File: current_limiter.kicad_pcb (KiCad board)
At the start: 4 copper layers, 83.9 x 37.5 mm, 49 parts, among them J1 73096-2, J2 73096-2, J3 CS-, J4 CS+, J5 73096-2, J6 73096-2, Q1 BSC040N10NS5, Q2 BC849, Q3 BC858, U1 TLV1805QDBVRQ1, U2 INA181A2IDBVR, U3 OPA991IDCKR, U4 BAT54CLT3G, U5 LM4040DIM3-2.5/NOPB

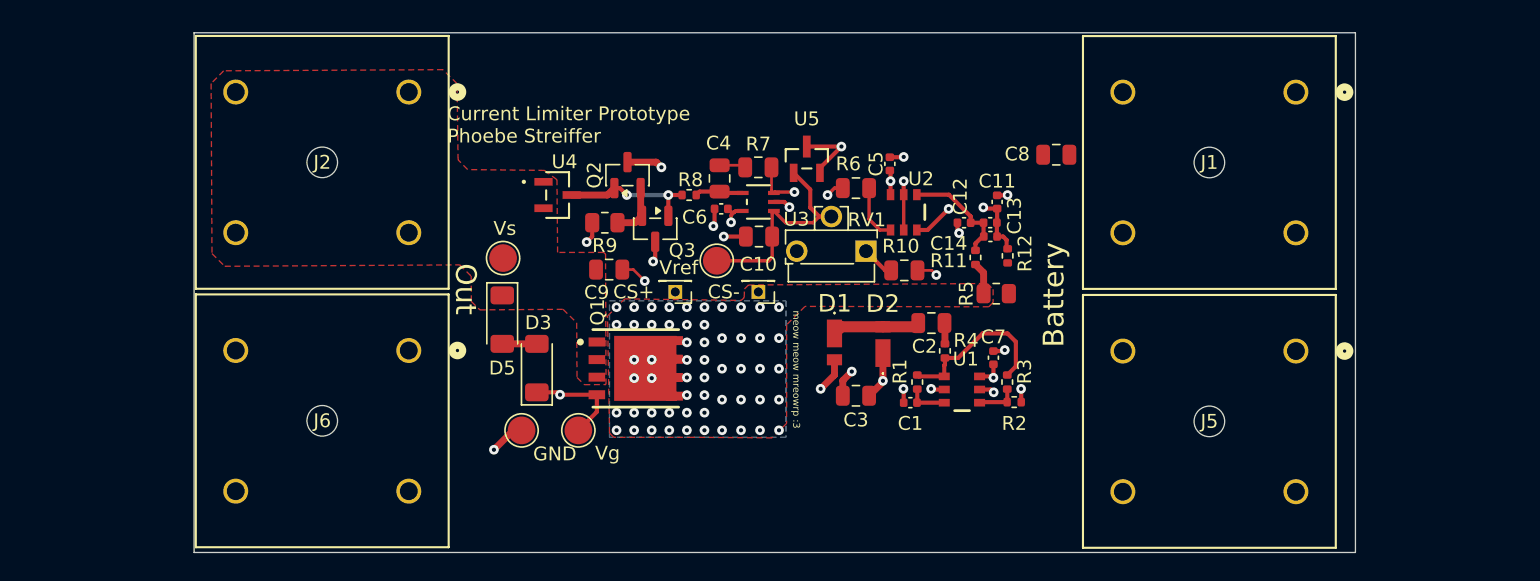
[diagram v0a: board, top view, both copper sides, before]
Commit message: minor revisions: added mounting holes, changed one track to back signal layer
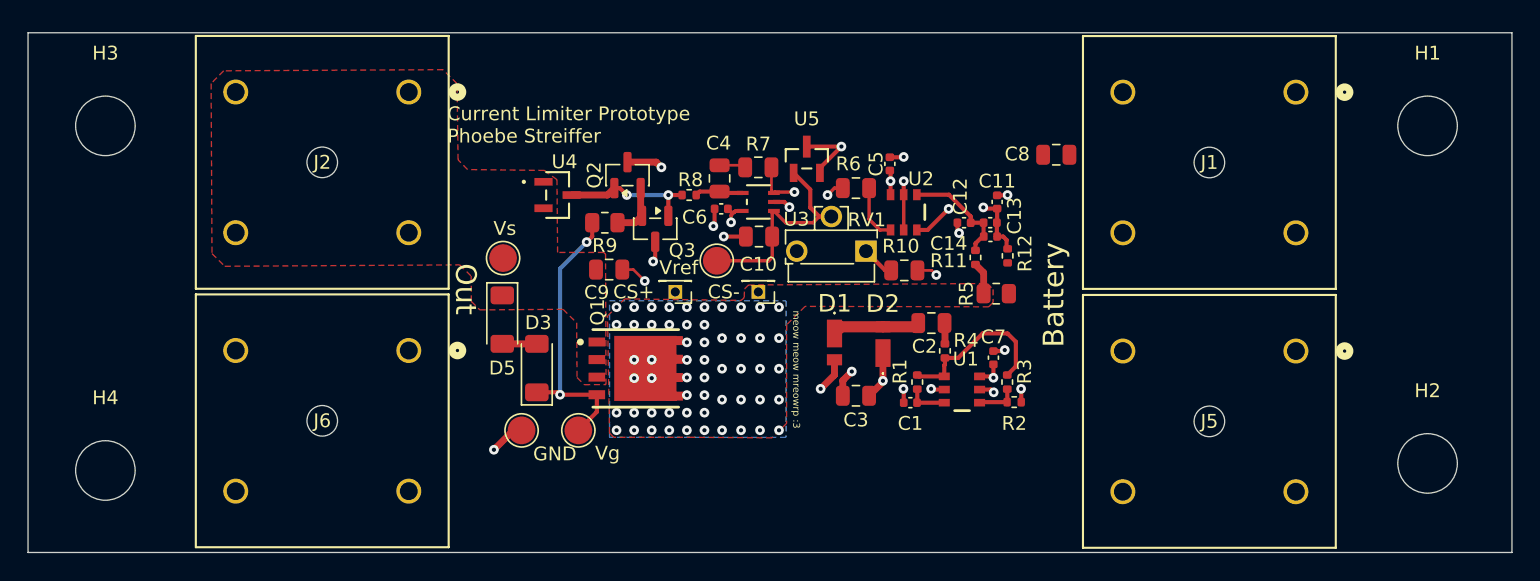
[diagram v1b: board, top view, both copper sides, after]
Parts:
- added H1: MountingHole, MountingHole:MountingHole_4.3mm_M4, F.Cu at (180.3, 32.0)
- added H2: MountingHole, MountingHole:MountingHole_4.3mm_M4, F.Cu at (180.3, 56.4)
- added H3: MountingHole, MountingHole:MountingHole_4.3mm_M4, F.Cu at (84.8, 32.0)
- added H4: MountingHole, MountingHole:MountingHole_4.3mm_M4, F.Cu at (84.8, 56.9)
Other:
- board size 83.9 x 37.5 mm -> 107.2 x 37.5 mm

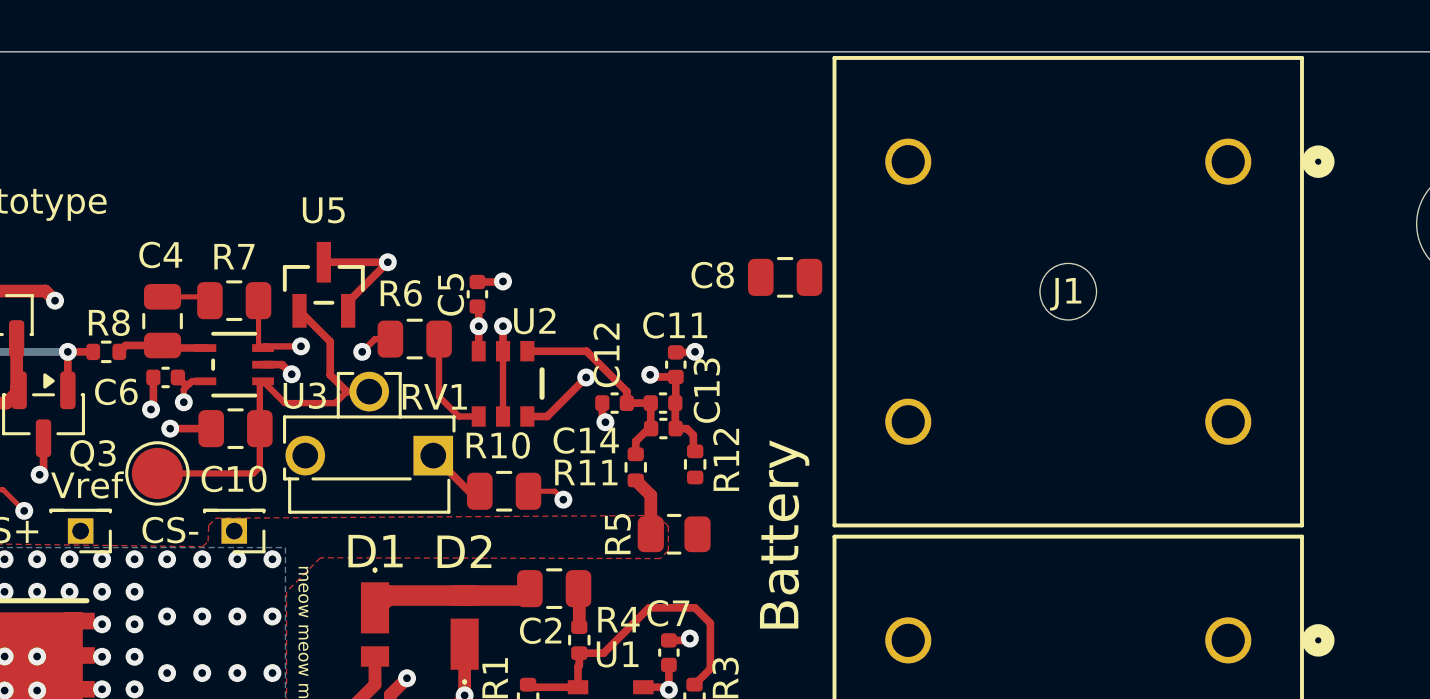
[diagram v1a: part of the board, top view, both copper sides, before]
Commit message: proper shunt setup, properly calculated resistance values necessary for shunt diode to operate safely
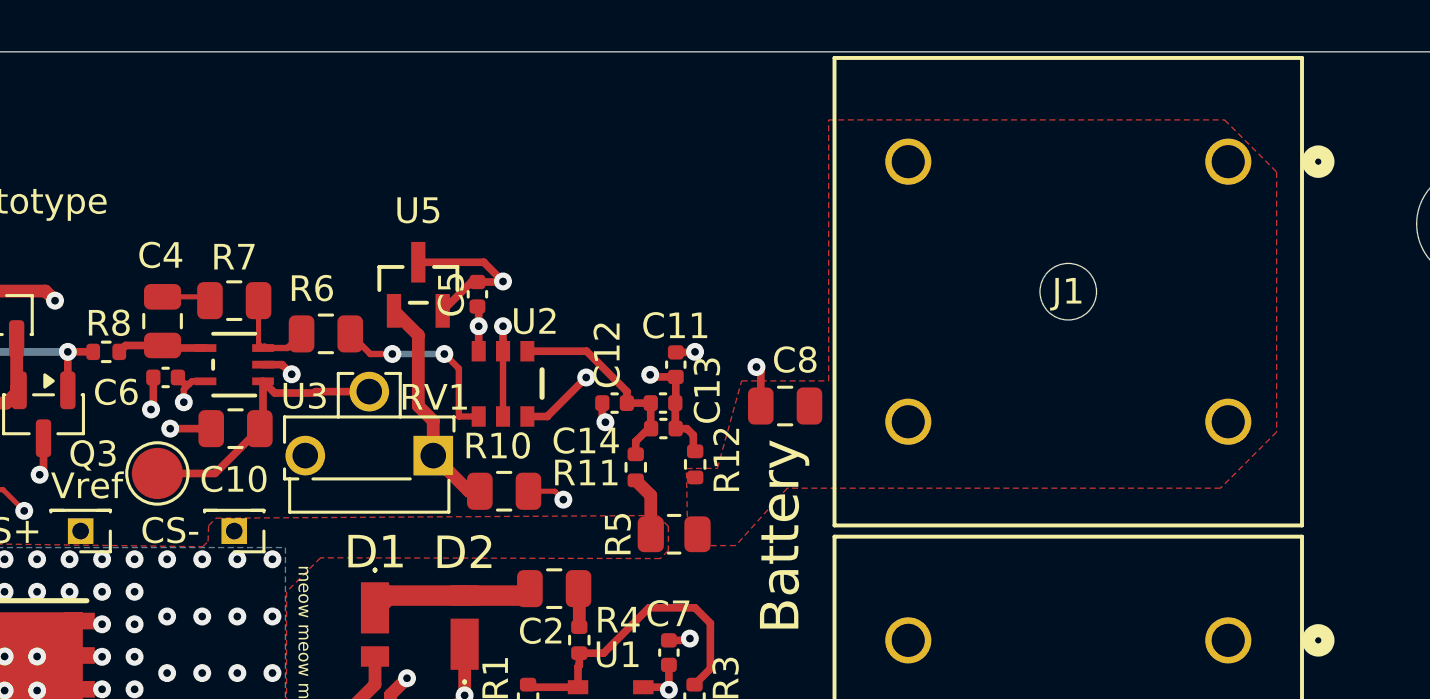
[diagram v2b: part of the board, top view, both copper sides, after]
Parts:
- R10: value 50k -> 20k
- moved C8 5.03 mm to (153.5, 39.1)
- moved U5 3.69 mm to (139.2, 34.4)
- moved R6 3.48 mm to (135.6, 36.3)
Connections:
- C10 pad 2: /REF_SET -> Net-(U3-IN+)
- RV1 pad 2: /REF_SET -> Net-(U3-IN+)
- TP3 pad 1: /REF_SET -> Net-(U3-IN+)
- U3 pad 1: /REF_SET -> Net-(U3-IN+)
- U5 pad 1: /REF_SET -> Net-(R10-Pad1)
- U5 pad 3: unconnected-(U5-Pad3) -> GND
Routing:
- net /REF_SET: track 16.1 -> 0.00 mm
- net Net-(U3-IN+): track 0.00 -> 11.0 mm
- net Net-(R10-Pad1): track 2.71 -> 10.3 mm
- net /PI_IN-: track 7.72 -> 3.75 mm, vias 2 -> 0
- net /CS_OUT: track 4.12 -> 7.45 mm, vias 0 -> 2
- net GND: track 27.7 -> 29.7 mm
- added copper zone on F.Cu, net +15V

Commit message: minor update: changed resistor value from 20k to 22k for E12 value
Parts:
- R10: value 20k -> 22k
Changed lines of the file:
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@@
 			)
 		)
-		(property "Value" "20k"
+		(property "Value" "22k"
 			(at 0 1.68 0)
 			(layer "F.Fab")

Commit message: minor updates: swapped out currentsense for in stock version, made sure all parts in stock, corrected Vs for currentsense
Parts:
- added R13: 22k, Capacitor_SMD:C_0805_2012Metric, F.Cu at (147.4, 34.0)
- added U6: LM4040DIM3-5.0/NOPB, Current_Limiter_Stuff:DBZ3, F.Cu at (143.9, 30.7)
- Q1: value BSC040N10NS5 -> ISC025N08NM5LF2
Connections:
- C5 pad 1: +15V -> Net-(U2-V+)
- U2 pad 6: +15V -> Net-(U2-V+)
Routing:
- net Net-(U2-V+): track 0.00 -> 10.2 mm
- net GND: track 29.7 -> 35.6 mm, vias 17 -> 18

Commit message: updated zeners to model thats actually in stock
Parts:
- removed D3, D5: BZV55B20, Diode_SMD:D_MiniMELF
- added CR1: BZT52C20-7-F, Current_Limiter_Stuff:SOD123_DIO, F.Cu at (113.5, 46.0)
- added CR2: BZT52C20-7-F, Current_Limiter_Stuff:SOD123_DIO, F.Cu at (115.8, 49.6)
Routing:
- net Net-(D3-A): track 2.50 -> 0.00 mm
- net Net-(CR1-Pad2): track 0.00 -> 2.50 mm

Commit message: updated all passive components to 805 footprint, added 3V3 regulator for currentsense
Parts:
- removed C5: 10n, Capacitor_SMD:C_0402_1005Metric
- added C16: 100n, Capacitor_SMD:C_0805_2012Metric, F.Cu at (149.9, 30.0)
- added C17: 100p, Capacitor_SMD:C_0805_2012Metric, F.Cu at (153.9, 34.0)
- added C18: 22u, Capacitor_SMD:C_0805_2012Metric, F.Cu at (143.8, 30.0)
- added C19: 22u, Capacitor_SMD:C_0805_2012Metric, F.Cu at (145.8, 30.0)
- added C20: 100n, Capacitor_SMD:C_0805_2012Metric, F.Cu at (140.2, 35.1)
- added L1: 10u, Inductor_SMD:L_0805_2012Metric, F.Cu at (147.8, 30.0)
- added R14: 22k, Resistor_SMD:R_0805_2012Metric, F.Cu at (139.7, 32.0)
- added R15: 10k, Resistor_SMD:R_0805_2012Metric, F.Cu at (142.5, 41.8)
- C1, C11, C12, C13, C14, C6, C7: footprint Capacitor_SMD:C_0402_1005Metric -> Capacitor_SMD:C_0805_2012Metric
- R1, R11, R12, R2, R3, R4, R8: footprint Resistor_SMD:R_0402_1005Metric -> Resistor_SMD:R_0805_2012Metric
- R10: value 22k -> 30.1k; footprint Capacitor_SMD:C_0805_2012Metric -> Resistor_SMD:R_0805_2012Metric
- R13: value 22k -> 158k; footprint Capacitor_SMD:C_0805_2012Metric -> Resistor_SMD:R_0805_2012Metric
- R6, R7: footprint Capacitor_SMD:C_0805_2012Metric -> Resistor_SMD:R_0805_2012Metric
- U2: value INA181A2IDBVR -> ZXCT181A2W6-7
- U6: value LM4040DIM3-5.0/NOPB -> AP63203QWU-7; footprint Current_Limiter_Stuff:DBZ3 -> Current_Limiter_Stuff:TSOT26_DIO
- moved R10 12.1 mm to (153.4, 37.1), turned to 180 degrees
- moved U6 9.07 mm to (152.9, 30.3), turned to 180 degrees
- moved U5 5.64 mm to (137.7, 29.0), turned to 90 degrees
- moved C12 5.29 mm to (146.8, 33.7), turned to -90 degrees
- moved R13 4.51 mm to (151.9, 34.0), turned to 90 degrees
- moved C11 3.81 mm to (148.8, 33.7)
- moved C14 3.42 mm to (148.8, 36.6)
- moved C1 3.40 mm to (144.2, 55.2), turned to 180 degrees
- moved C7 3.30 mm to (151.9, 50.3), turned to -90 degrees
- moved R3 3.17 mm to (149.5, 53.6), turned to -90 degrees
- moved R4 2.43 mm to (147.8, 47.6)
- moved R2 2.37 mm to (152.4, 53.3)
- moved C4 2.22 mm to (130.6, 34.0)
- moved R1 1.91 mm to (142.9, 52.3)
- moved R8 1.53 mm to (127.5, 35.6)
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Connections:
- R10 pad 1: Net-(R10-Pad1) -> Net-(U6-FB)
- R10 pad 2: +15V -> GND
- R13 pad 1: Net-(U2-V+) -> +3V3
- R13 pad 2: +15V -> Net-(U6-FB)
- RV1 pad 1: Net-(R10-Pad1) -> Net-(R15-Pad1)
- U2 pad 6: Net-(U2-V+) -> +3V3
- U5 pad 1: Net-(R10-Pad1) -> Net-(R14-Pad2)
- U6 pad 1: Net-(U2-V+) -> Net-(U6-FB)
- U6 pad 2: GND -> +15V
- U6 pad 3: GND -> +15V
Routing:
- net +3V3: track 0.00 -> 22.2 mm
- net Net-(R14-Pad2): track 0.00 -> 15.2 mm, vias 0 -> 2
- net Net-(R10-Pad1): track 10.3 -> 0.00 mm
- net Net-(U2-V+): track 10.2 -> 0.00 mm
- net Net-(U6-FB): track 0.00 -> 8.74 mm
- net /CS_FILTERED+: track 10.4 -> 17.5 mm
- net /OSC_OUT: track 12.1 -> 18.2 mm, vias 0 -> 2
- net GND: track 35.6 -> 41.6 mm, vias 18 -> 19
- net Net-(U6-SW): track 0.00 -> 4.38 mm
- net Net-(R15-Pad1): track 0.00 -> 4.22 mm
- net /CS_FILTERED-: track 8.03 -> 10.6 mm
- net Net-(U6-BST): track 0.00 -> 1.88 mm
- net +15V: track 7.29 -> 9.17 mm, vias 4 -> 3
- net /BASE: track 9.89 -> 11.4 mm
- net /OSC_IN+: track 2.96 -> 4.38 mm
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
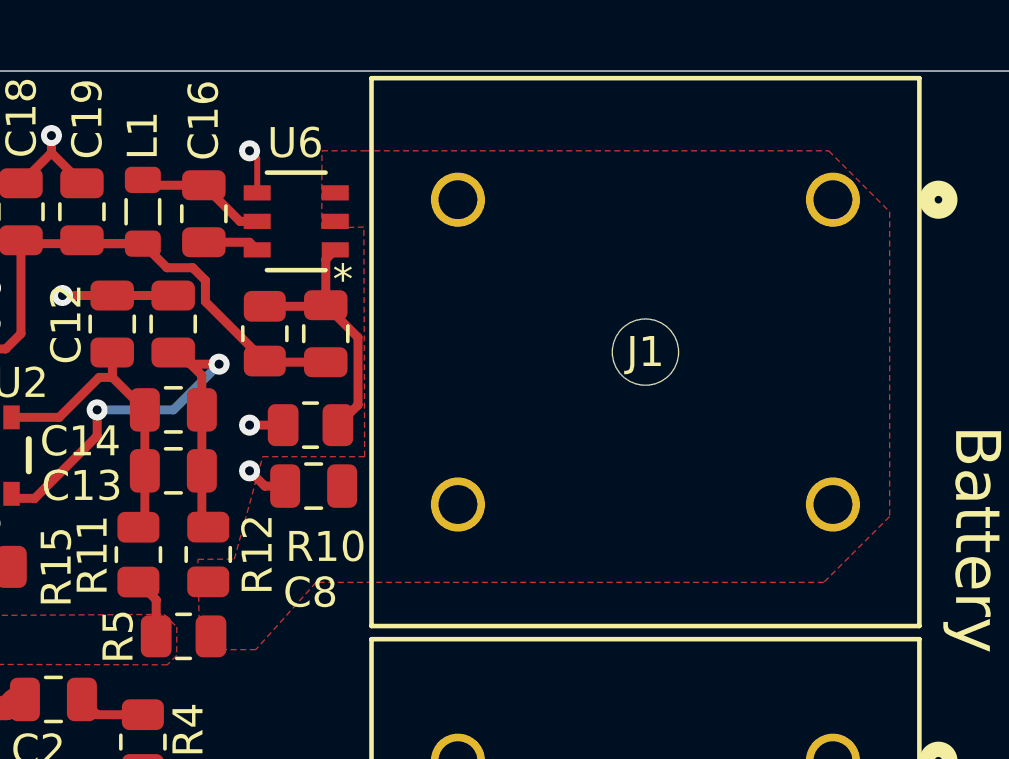
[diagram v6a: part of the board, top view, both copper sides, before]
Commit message: updated 3v3 reg to be correct ala datasheet
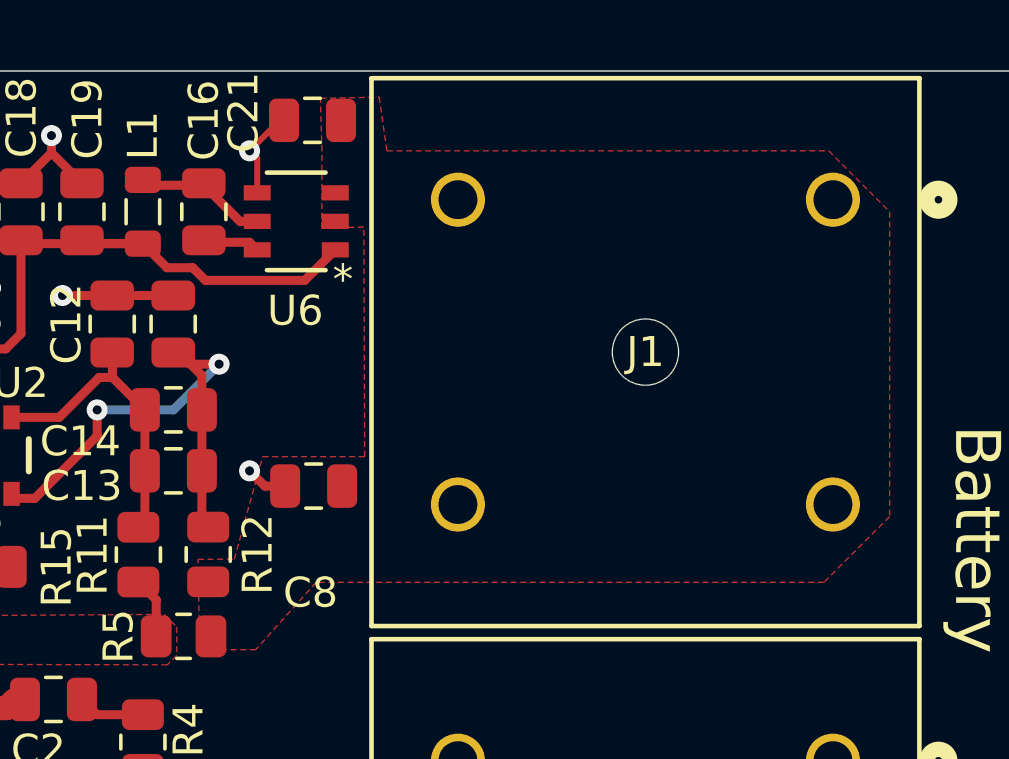
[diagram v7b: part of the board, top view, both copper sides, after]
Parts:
- removed C17: 100p, Capacitor_SMD:C_0805_2012Metric
- removed R10: 30.1k, Resistor_SMD:R_0805_2012Metric
- removed R13: 158k, Resistor_SMD:R_0805_2012Metric
- added C21: 10u, Capacitor_SMD:C_0805_2012Metric, F.Cu at (153.5, 26.9)
- moved C16 0.07 mm to (149.9, 30.0)
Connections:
- net Net-(U3-IN+) renamed /REF_SET
- U6 pad 1: Net-(U6-FB) -> +3V3
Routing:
- net Net-(U6-FB): track 8.74 -> 0.00 mm
- net +3V3: track 22.2 -> 21.4 mm
- net GND: track 41.6 -> 42.0 mm, vias 19 -> 18

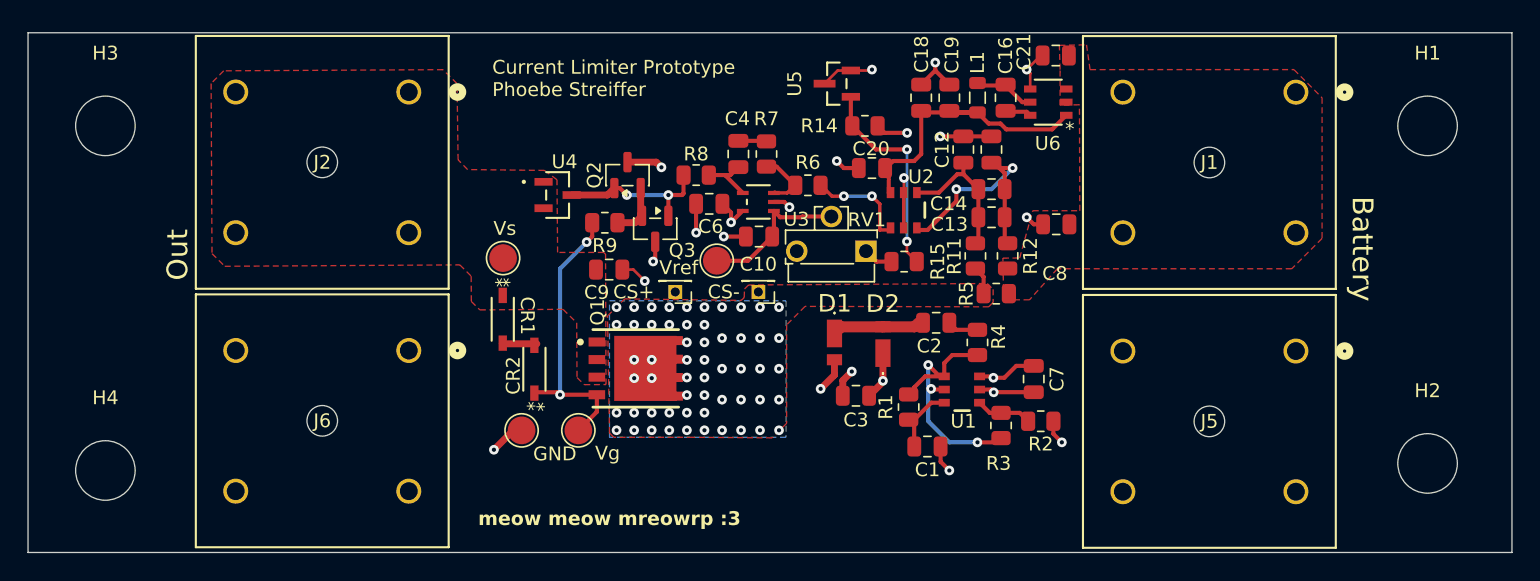
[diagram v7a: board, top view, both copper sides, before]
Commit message: minor changes including changing to more viable inductor footprint & correct inductor sizing
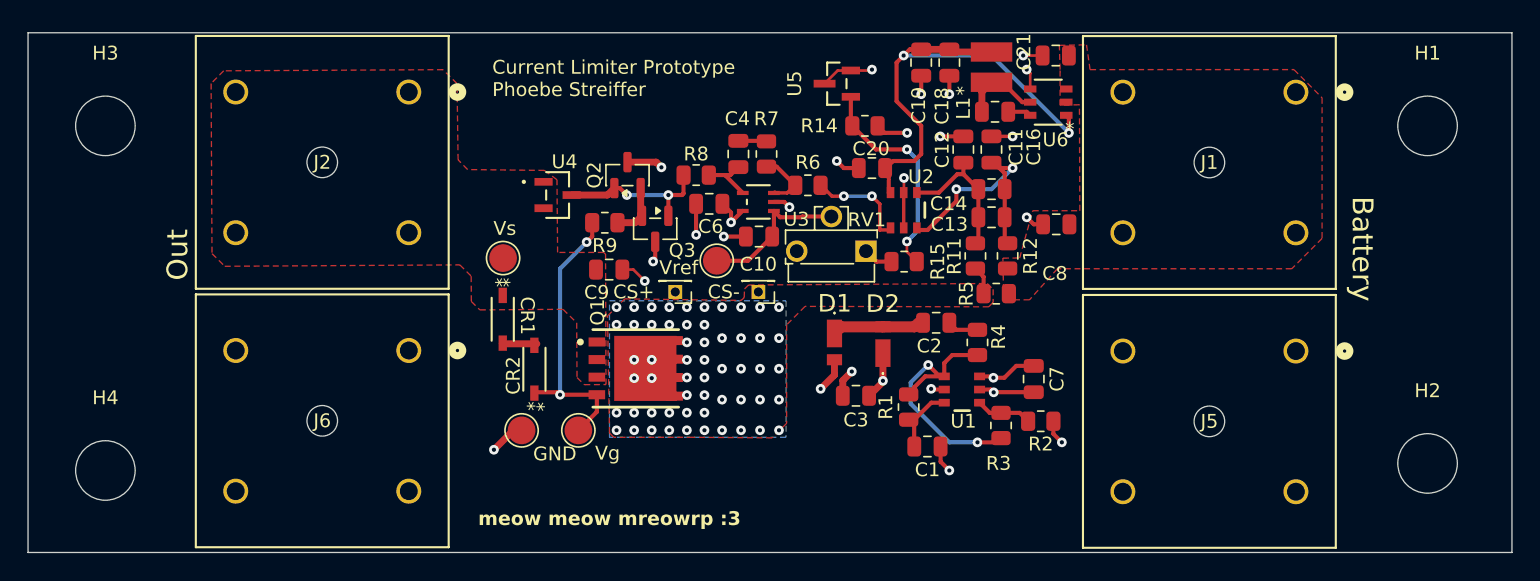
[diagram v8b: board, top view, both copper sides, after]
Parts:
- L1: value 10u -> 3u3; footprint Inductor_SMD:L_0805_2012Metric -> Current_Limiter_Stuff:IND_BOURNS_SDR0302
- moved C18 3.25 mm to (145.8, 27.4), turned to -90 degrees
- moved C19 3.25 mm to (143.8, 27.4), turned to -90 degrees
- moved L1 2.43 mm to (148.8, 27.8), turned to 90 degrees
- moved C16 1.27 mm to (149.1, 31.0), turned to 180 degrees
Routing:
- net +3V3: track 21.4 -> 35.0 mm, vias 0 -> 2
- net GND: track 42.0 -> 40.6 mm, vias 18 -> 21
- net /OSC_OUT: track 18.2 -> 19.3 mm
- net Net-(R14-Pad2): track 15.2 -> 15.8 mm
- net VCC: track 59.1 -> 59.6 mm
